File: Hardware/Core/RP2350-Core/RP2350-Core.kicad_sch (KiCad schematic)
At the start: 0 parts

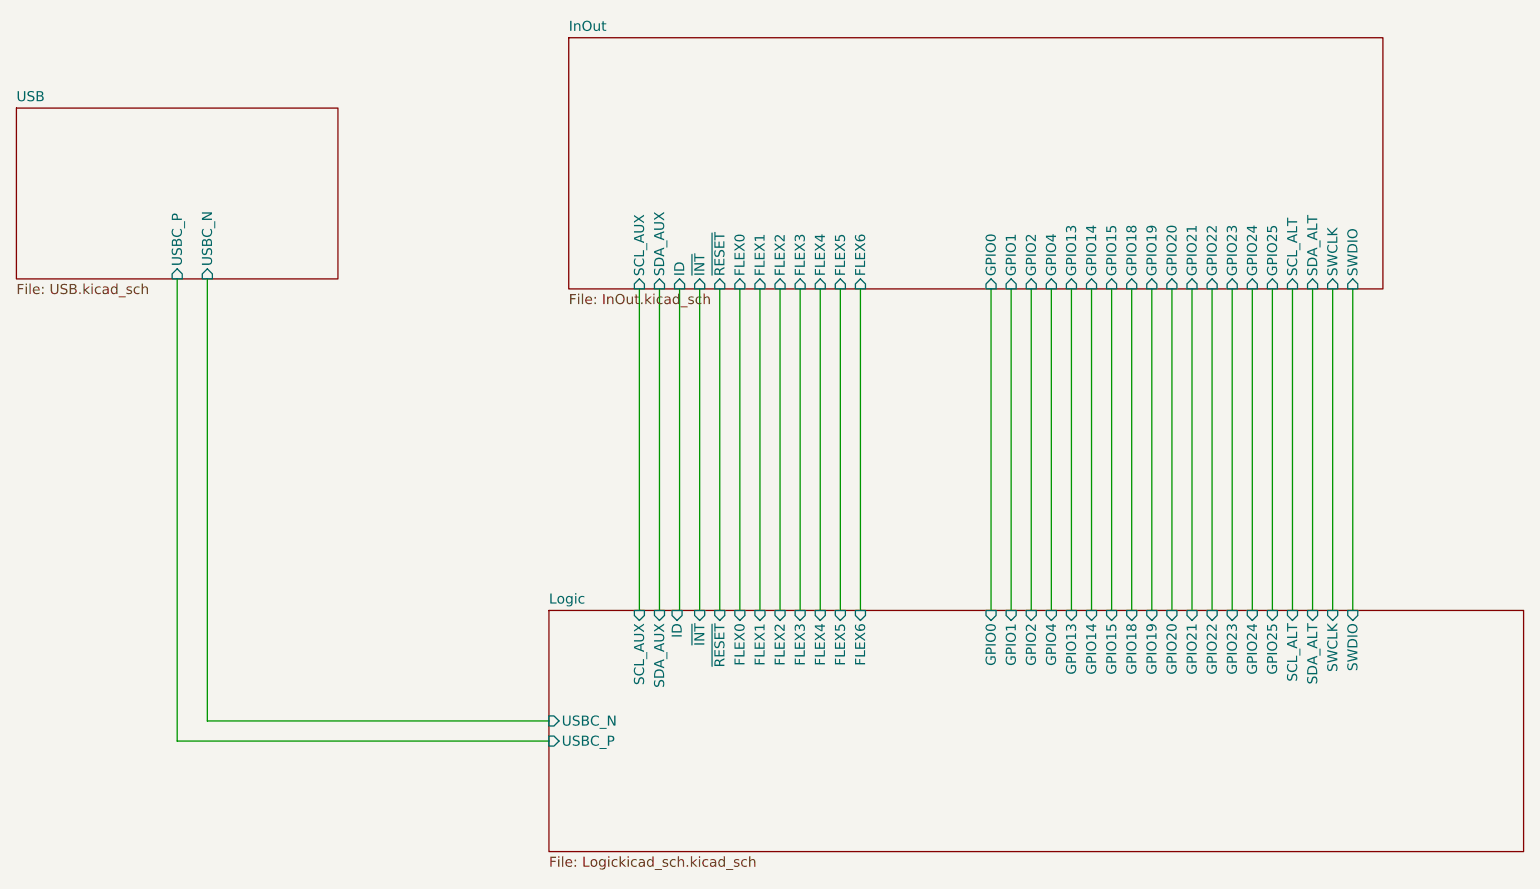
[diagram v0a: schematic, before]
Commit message: Added RP2354 with integrated flash, 80 pin and OR diode in power supply
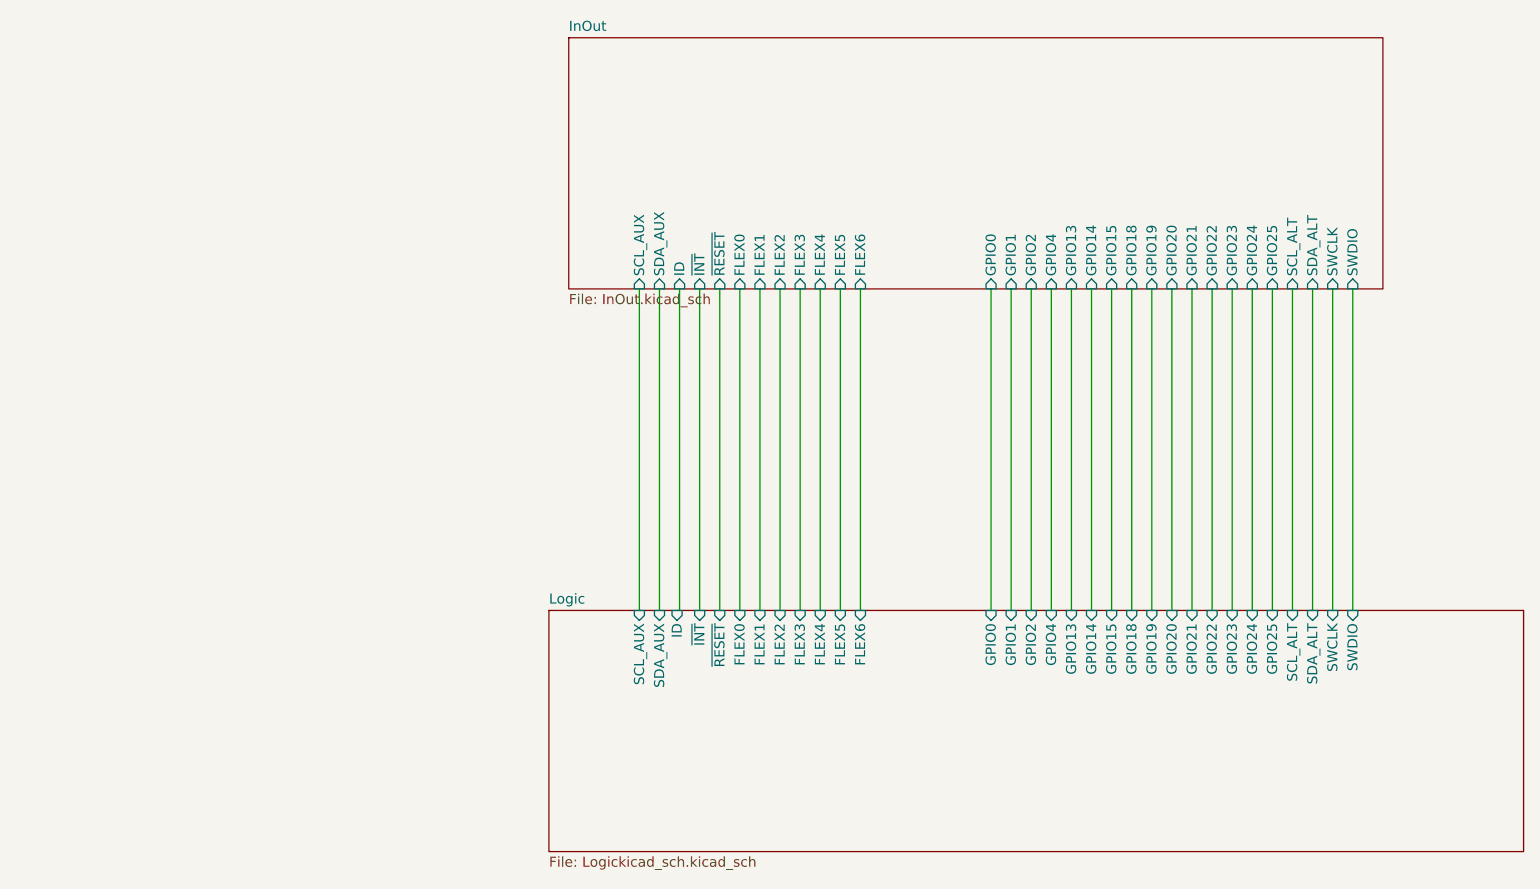
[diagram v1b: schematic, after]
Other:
- removed sheet USB
- sheet Logic ports: added none; removed USBC_N, USBC_P
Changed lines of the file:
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@@
-	(wire
-		(pts
-			(xy 72.39 114.3) (xy 119.38 114.3)
-		)
-		(stroke
-			(width 0)
-			(type default)
-		)
-	)
 	(wire
 		(pts
@@
 	(wire
 		(pts
-			(xy 76.2 111.76) (xy 119.38 111.76)
-		)
-		(stroke
-			(width 0)
-			(type default)
-		)
-	)
-	(wire
-		(pts
-			(xy 72.39 55.88) (xy 72.39 114.3)
-		)
-		(stroke
-			(width 0)
-			(type default)
-		)
-	)
-	(wire
-		(pts
 			(xy 140.97 57.15) (xy 140.97 97.79)
-		)
-		(stroke
-			(width 0)
-			(type default)
-		)
-	)
-	(wire
-		(pts
-			(xy 76.2 55.88) (xy 76.2 111.76)
 		)
 		(stroke
@@
 	)
 	(sheet
-		(at 52.07 34.29)
-		(size 40.64 21.59)
-		(exclude_from_sim no)
-		(in_bom yes)
-		(on_board yes)
-		(dnp no)
-		(fields_autoplaced yes)
-		(stroke
-			(width 0.1524)
-			(type solid)
-		)
-		(fill
-			(color 0 0 0 0)
-		)
-		(property "Sheetname" "USB"
-			(at 52.07 33.5784 0)
-			(show_name no)
-			(do_not_autoplace no)
-			(effects
-				(font
-					(size 1.27 1.27)
-				)
-				(justify left bottom)
-			)
-		)
-		(property "Sheetfile" "USB.kicad_sch"
-			(at 52.07 56.4646 0)
-			(show_name no)
-			(do_not_autoplace no)
-			(effects
-				(font
-					(size 1.27 1.27)
-				)
-				(justify left top)
-			)
-		)
-		(pin "USBC_N" input
-			(at 76.2 55.88 270)
-			(effects
-				(font
-					(size 1.27 1.27)
-				)
-				(justify left)
-			)
-		)
-		(pin "USBC_P" input
-			(at 72.39 55.88 270)
-			(effects
-				(font
-					(size 1.27 1.27)
-				)
-				(justify left)
-			)
-		)
-		(instances
-			(project "RP2350-Core"
-				(path "/8bfb0932-e2fe-4425-80ff-903dfd664561"
-					(page "3")
-				)
-			)
-		)
-	)
-	(sheet
 		(at 119.38 97.79)
 		(size 123.19 30.48)
@@
 			)
 		)
-		(pin "USBC_N" input
-			(at 119.38 111.76 180)
-			(effects
-				(font
-					(size 1.27 1.27)
-				)
-				(justify left)
-			)
-		)
-		(pin "USBC_P" input
-			(at 119.38 114.3 180)
-			(effects
-				(font
-					(size 1.27 1.27)
-				)
-				(justify left)
-			)
-		)
